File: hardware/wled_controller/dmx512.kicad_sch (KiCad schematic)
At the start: 12 parts, among them J18 NC3MAH, J19 NC3FAH, U10 TLV74333, U9 ISO35T

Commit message: finalise schematic
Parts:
- U9: Shop (none) -> https://eu.mouser.com/ProductDetail/Texas-Instruments/ISO35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
- renumbered J18 to J21, J19 to J22
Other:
- note added: "TODO: decide whether to use 3-pin or 5-pin connectors"
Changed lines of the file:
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@@
+	)
+	(junction
+		(at 114.3 80.01)
+		(diameter 0)
+		(color 0 0 0 0)
 	)
 	(junction
@@
 	)
 	(junction
+		(at 132.08 60.96)
+		(diameter 0)
+		(color 0 0 0 0)
+	)
+	(junction
 		(at 121.92 111.76)
 		(diameter 0)
@@
 	(wire
 		(pts
+			(xy 114.3 80.01) (xy 110.49 80.01)
+		)
+		(stroke
+			(width 0)
+			(type default)
+		)
+	)
+	(wire
+		(pts
 			(xy 185.42 60.96) (xy 180.34 60.96)
 		)
@@
 	(wire
 		(pts
-			(xy 137.16 80.01) (xy 110.49 80.01)
+			(xy 137.16 80.01) (xy 114.3 80.01)
 		)
 		(stroke
@@
 	(wire
 		(pts
+			(xy 114.3 78.74) (xy 114.3 80.01)
+		)
+		(stroke
+			(width 0)
+			(type default)
+		)
+	)
+	(wire
+		(pts
 			(xy 77.47 109.22) (xy 77.47 85.09)
 		)
@@
 	(wire
 		(pts
+			(xy 130.81 60.96) (xy 132.08 60.96)
+		)
+		(stroke
+			(width 0)
+			(type default)
+		)
+	)
+	(wire
+		(pts
 			(xy 90.17 129.54) (xy 91.44 129.54)
 		)
@@
 			(width 0)
 			(type default)
+		)
+	)
+	(text "TODO: decide whether to use 3-pin or 5-pin connectors"
+		(exclude_from_sim no)
+		(at 222.25 38.1 0)
+		(effects
+			(font
+				(size 1.27 1.27)
+			)
 		)
 	)
@@
 			)
 			(justify right)
+		)
+	)
+	(symbol
+		(lib_id "power:PWR_FLAG")
+		(at 114.3 78.74 0)
+		(unit 1)
+		(exclude_from_sim no)
+		(in_bom yes)
+		(on_board yes)
+		(dnp no)
+		(fields_autoplaced yes)
+		(property "Reference" "#FLG06"
+			(at 114.3 76.835 0)
+			(effects
+				(font
+					(size 1.27 1.27)
+				)
+				(hide yes)
+			)
+		)
+		(property "Value" "PWR_FLAG"
+			(at 114.3 73.66 0)
+			(effects
+				(font
+					(size 1.27 1.27)
+				)
+				(hide yes)
+			)
+		)
+		(property "Footprint" ""
+			(at 114.3 78.74 0)
+			(effects
+				(font
+					(size 1.27 1.27)
+				)
+				(hide yes)
+			)
+		)
+		(property "Datasheet" "~"
+			(at 114.3 78.74 0)
+			(effects
+				(font
+					(size 1.27 1.27)
+				)
+				(hide yes)
+			)
+		)
+		(property "Description" "Special symbol for telling ERC where power comes from"
+			(at 114.3 78.74 0)
+			(effects
+				(font
+					(size 1.27 1.27)
+				)
+				(hide yes)
+			)
+		)
+		(pin "1"
+		)
+		(instances
+			(project "wled_controller"
+				(path "/67a034fd-c582-46b2-83e2-3de9f5f70ac4/ded7ca3b-172a-4291-b42a-ac8e31eb8d0c"
+					(reference "#FLG06")
+					(unit 1)
+				)
+			)
 		)
 	)
@@
 		(dnp no)
 		(fields_autoplaced yes)
-		(property "Reference" "#PWR091"
+		(property "Reference" "#PWR097"
 			(at 39.37 97.79 0)
 			(effects
@@
 			(project "wled_controller"
 				(path "/67a034fd-c582-46b2-83e2-3de9f5f70ac4/ded7ca3b-172a-4291-b42a-ac8e31eb8d0c"
-					(reference "#PWR091")
+					(reference "#PWR097")
 					(unit 1)
 				)
@@
 		(dnp no)
 		(fields_autoplaced yes)
-		(property "Reference" "J18"
+		(property "Reference" "J21"
 			(at 227.33 49.53 0)
 			(effects
@@
 			(project ""
 				(path "/67a034fd-c582-46b2-83e2-3de9f5f70ac4/ded7ca3b-172a-4291-b42a-ac8e31eb8d0c"
-					(reference "J18")
+					(reference "J21")
 					(unit 1)
 				)
@@
 		(on_board yes)
 		(dnp no)
-		(property "Reference" "#PWR090"
+		(property "Reference" "#PWR096"
 			(at 39.37 82.55 0)
 			(effects
@@
 			(project "wled_controller"
 				(path "/67a034fd-c582-46b2-83e2-3de9f5f70ac4/ded7ca3b-172a-4291-b42a-ac8e31eb8d0c"
-					(reference "#PWR090")
+					(reference "#PWR096")
 					(unit 1)
 				)
@@
 		(dnp no)
 		(fields_autoplaced yes)
-		(property "Reference" "#PWR095"
+		(property "Reference" "#PWR0101"
 			(at 83.82 129.54 0)
 			(effects
@@
 			(project "wled_controller"
 				(path "/67a034fd-c582-46b2-83e2-3de9f5f70ac4/ded7ca3b-172a-4291-b42a-ac8e31eb8d0c"
-					(reference "#PWR095")
+					(reference "#PWR0101")
 					(unit 1)
 				)
@@
 	)
 	(symbol
+		(lib_id "power:PWR_FLAG")
+		(at 130.81 60.96 90)
+		(unit 1)
+		(exclude_from_sim no)
+		(in_bom yes)
+		(on_board yes)
+		(dnp no)
+		(fields_autoplaced yes)
+		(property "Reference" "#FLG07"
+			(at 128.905 60.96 0)
+			(effects
+				(font
+					(size 1.27 1.27)
+				)
+				(hide yes)
+			)
+		)
+		(property "Value" "PWR_FLAG"
+			(at 125.73 60.96 0)
+			(effects
+				(font
+					(size 1.27 1.27)
+				)
+				(hide yes)
+			)
+		)
+		(property "Footprint" ""
+			(at 130.81 60.96 0)
+			(effects
+				(font
+					(size 1.27 1.27)
+				)
+				(hide yes)
+			)
+		)
+		(property "Datasheet" "~"
+			(at 130.81 60.96 0)
+			(effects
+				(font
+					(size 1.27 1.27)
+				)
+				(hide yes)
+			)
+		)
+		(property "Description" "Special symbol for telling ERC where power comes from"
+			(at 130.81 60.96 0)
+			(effects
+				(font
+					(size 1.27 1.27)
+				)
+				(hide yes)
+			)
+		)
+		(pin "1"
+		)
+		(instances
+			(project "wled_controller"
+				(path "/67a034fd-c582-46b2-83e2-3de9f5f70ac4/ded7ca3b-172a-4291-b42a-ac8e31eb8d0c"
+					(reference "#FLG07")
+					(unit 1)
+				)
+			)
+		)
+	)
+	(symbol
 		(lib_id "power:+3.3V")
 		(at 88.9 80.01 90)
@@
 		(dnp no)
 		(fields_autoplaced yes)
-		(property "Reference" "#PWR092"
+		(property "Reference" "#PWR098"
 			(at 92.71 80.01 0)
 			(effects
@@
 			(project "wled_controller"
 				(path "/67a034fd-c582-46b2-83e2-3de9f5f70ac4/ded7ca3b-172a-4291-b42a-ac8e31eb8d0c"
-					(reference "#PWR092")
+					(reference "#PWR098")
 					(unit 1)
 				)
@@
 		(dnp no)
 		(fields_autoplaced yes)
-		(property "Reference" "#PWR093"
+		(property "Reference" "#PWR099"
 			(at 92.71 104.14 0)
 			(effects
@@
 			(project ""
 				(path "/67a034fd-c582-46b2-83e2-3de9f5f70ac4/ded7ca3b-172a-4291-b42a-ac8e31eb8d0c"
-					(reference "#PWR093")
+					(reference "#PWR099")
 					(unit 1)
 				)
@@
 		(dnp no)
 		(fields_autoplaced yes)
-		(property "Reference" "J19"
+		(property "Reference" "J22"
 			(at 227.33 74.93 0)
 			(effects
@@
 			(project ""
 				(path "/67a034fd-c582-46b2-83e2-3de9f5f70ac4/ded7ca3b-172a-4291-b42a-ac8e31eb8d0c"
-					(reference "J19")
+					(reference "J22")
 					(unit 1)
 				)
@@
 			)
 		)
+		(property "Shop" "https://eu.mouser.com/ProductDetail/Texas-Instruments/ISO35TDWR?qs=QtI0yD1FyONZngHt9P0v7A%3D%3D"
+			(at 105.41 101.6 0)
+			(effects
+				(font
+					(size 1.27 1.27)
+				)
+				(hide yes)
+			)
+		)
 		(pin "4"
 		)
@@
 		(dnp no)
 		(fields_autoplaced yes)
-		(property "Reference" "#PWR094"
+		(property "Reference" "#PWR0100"
 			(at 90.17 102.87 0)
 			(effects
@@
 			(project "wled_controller"
 				(path "/67a034fd-c582-46b2-83e2-3de9f5f70ac4/ded7ca3b-172a-4291-b42a-ac8e31eb8d0c"
-					(reference "#PWR094")
+					(reference "#PWR0100")
 					(unit 1)
 				)

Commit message: some progress on PCB
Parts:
- removed C13: 100nF, Capacitor_SMD:C_0805_2012Metric, symbol Device:C
- renumbered C14 to C13, C15 to C14, C16 to C15, C17 to C16, C18 to C17, D3 to D4

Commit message: work on pcb
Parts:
- renumbered C13 to C11, C14 to C12, C15 to C13, C16 to C14, C17 to C15
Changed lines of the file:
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@@
 		(on_board yes)
 		(dnp no)
-		(property "Reference" "C13"
+		(property "Reference" "C11"
 			(at 91.44 88.9 0)
 			(effects
@@
 			(project "wled_controller"
 				(path "/67a034fd-c582-46b2-83e2-3de9f5f70ac4/ded7ca3b-172a-4291-b42a-ac8e31eb8d0c"
-					(reference "C13")
+					(reference "C11")
 					(unit 1)
 				)
@@
 		(on_board yes)
 		(dnp no)
-		(property "Reference" "C14"
+		(property "Reference" "C12"
 			(at 138.43 67.31 0)
 			(effects
@@
 			(project "wled_controller"
 				(path "/67a034fd-c582-46b2-83e2-3de9f5f70ac4/ded7ca3b-172a-4291-b42a-ac8e31eb8d0c"
-					(reference "C14")
+					(reference "C12")
 					(unit 1)
 				)
@@
 		(on_board yes)
 		(dnp no)
-		(property "Reference" "C17"
+		(property "Reference" "C15"
 			(at 186.69 67.31 0)
 			(effects
@@
 			(project "wled_controller"
 				(path "/67a034fd-c582-46b2-83e2-3de9f5f70ac4/ded7ca3b-172a-4291-b42a-ac8e31eb8d0c"
-					(reference "C17")
+					(reference "C15")
 					(unit 1)
 				)
@@
 		(on_board yes)
 		(dnp no)
-		(property "Reference" "C15"
+		(property "Reference" "C13"
 			(at 148.59 67.31 0)
 			(effects
@@
 			(project "wled_controller"
 				(path "/67a034fd-c582-46b2-83e2-3de9f5f70ac4/ded7ca3b-172a-4291-b42a-ac8e31eb8d0c"
-					(reference "C15")
+					(reference "C13")
 					(unit 1)
 				)
@@
 		(on_board yes)
 		(dnp no)
-		(property "Reference" "C16"
+		(property "Reference" "C14"
 			(at 158.75 67.31 0)
 			(effects
@@
 			(project "wled_controller"
 				(path "/67a034fd-c582-46b2-83e2-3de9f5f70ac4/ded7ca3b-172a-4291-b42a-ac8e31eb8d0c"
-					(reference "C16")
+					(reference "C14")
 					(unit 1)
 				)
@@
 		(dnp no)
 		(fields_autoplaced yes)
-		(property "Reference" "#PWR099"
+		(property "Reference" "#PWR096"
 			(at 83.82 129.54 0)
 			(effects
@@
 			(project "wled_controller"
 				(path "/67a034fd-c582-46b2-83e2-3de9f5f70ac4/ded7ca3b-172a-4291-b42a-ac8e31eb8d0c"
-					(reference "#PWR099")
+					(reference "#PWR096")
 					(unit 1)
 				)
@@
 		(dnp no)
 		(fields_autoplaced yes)
-		(property "Reference" "#PWR096"
+		(property "Reference" "#PWR093"
 			(at 92.71 80.01 0)
 			(effects
@@
 			(project "wled_controller"
 				(path "/67a034fd-c582-46b2-83e2-3de9f5f70ac4/ded7ca3b-172a-4291-b42a-ac8e31eb8d0c"
-					(reference "#PWR096")
+					(reference "#PWR093")
 					(unit 1)
 				)
@@
 		(dnp no)
 		(fields_autoplaced yes)
-		(property "Reference" "#PWR097"
+		(property "Reference" "#PWR094"
 			(at 92.71 104.14 0)
 			(effects
@@
 			(project ""
 				(path "/67a034fd-c582-46b2-83e2-3de9f5f70ac4/ded7ca3b-172a-4291-b42a-ac8e31eb8d0c"
-					(reference "#PWR097")
+					(reference "#PWR094")
 					(unit 1)
 				)
@@
 		(dnp no)
 		(fields_autoplaced yes)
-		(property "Reference" "#PWR098"
+		(property "Reference" "#PWR095"
 			(at 90.17 102.87 0)
 			(effects
@@
 			(project "wled_controller"
 				(path "/67a034fd-c582-46b2-83e2-3de9f5f70ac4/ded7ca3b-172a-4291-b42a-ac8e31eb8d0c"
-					(reference "#PWR098")
-					(unit 1)
-				)
+					(reference "#PWR095")
+					(unit 1)
+				)

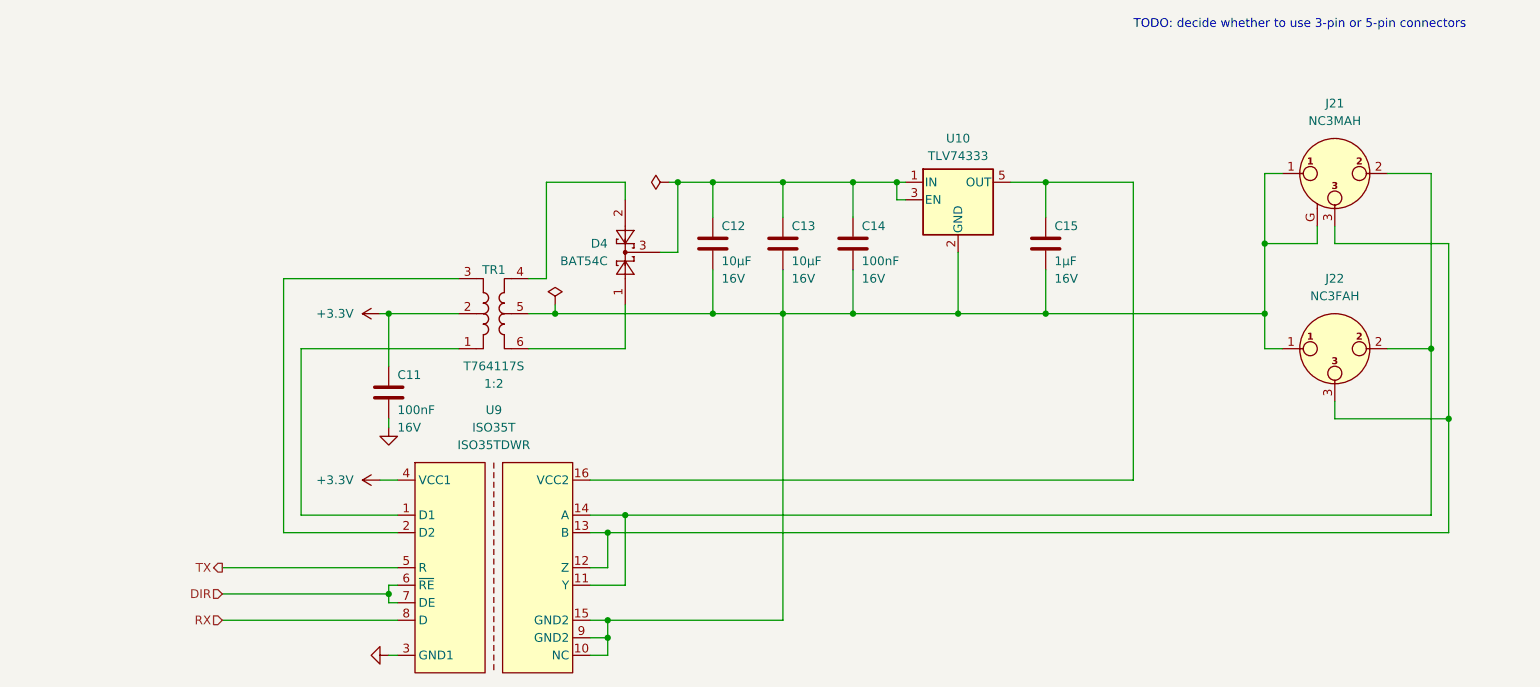
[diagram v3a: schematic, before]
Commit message: dmx512 line TVS
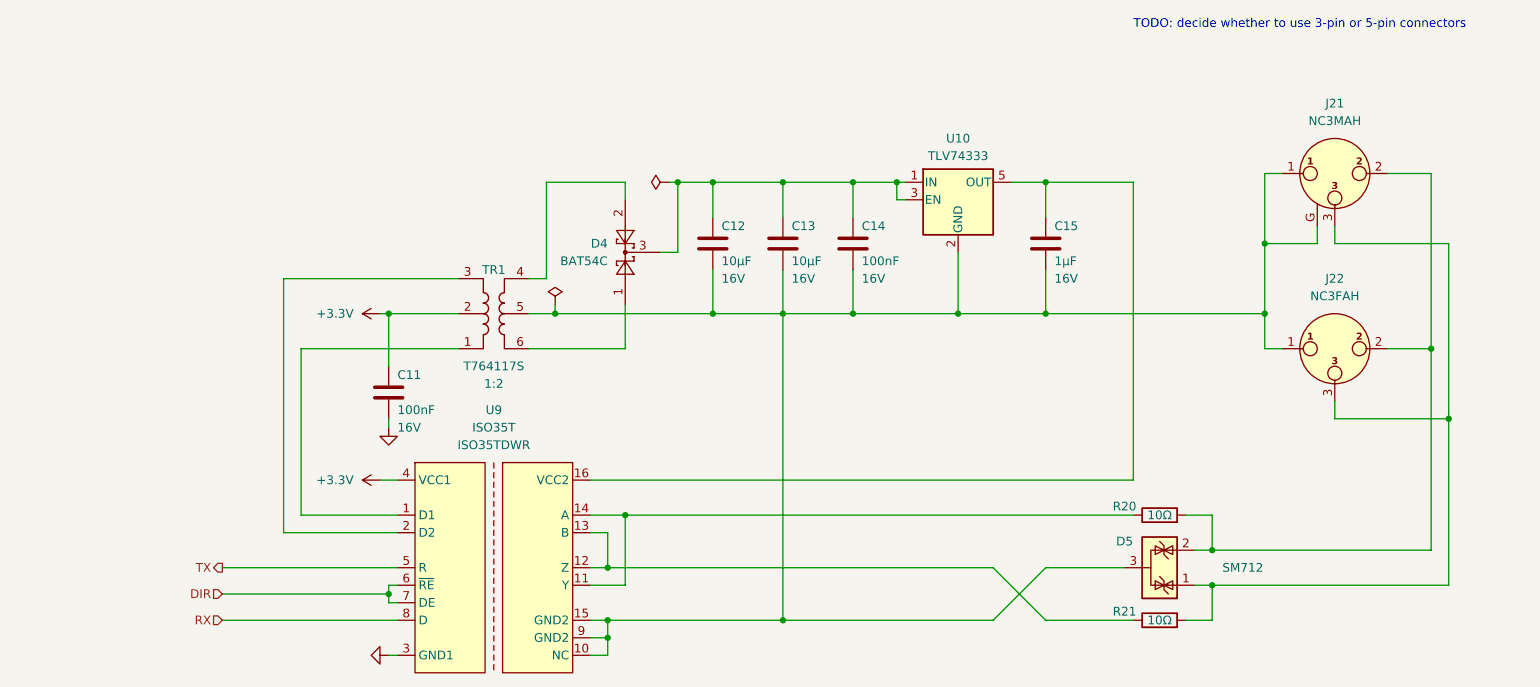
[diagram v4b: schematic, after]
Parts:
- added D5: SM712, Package_TO_SOT_SMD:SOT-23, symbol Power_Protection:NUP2105L
- added R20, R21: 10Ω, Resistor_SMD:R_0805_2012Metric, symbol Device:R
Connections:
- net at C12.2, C13.2, C14.2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: now also D5.3 (A)
- net at J21.2, J22.2: now also D5.2 (K), R20.2; no longer U9.11 (Y), U9.14 (A)
- net at J21.3, J22.3: now also D5.1 (K), R21.2; no longer U9.12 (Z), U9.13 (B)
- new net: R20.1, U9.11 (Y), U9.14 (A)
- new net: R21.1, U9.12 (Z), U9.13 (B)

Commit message: update bom
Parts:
- D5: Part (none) -> SM712
- R20, R21: Part (none) -> R 10Ω 125mW 5% 0805
- TR1: Part PAD001-T764120S -> PAD001-T764120S
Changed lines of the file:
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@@
 		)
 		(instances
-			(project ""
+			(project "wled_controller"
 				(path "/67a034fd-c582-46b2-83e2-3de9f5f70ac4/ded7ca3b-172a-4291-b42a-ac8e31eb8d0c"
 					(reference "J21")
@@
 		)
 		(property "Shop" "https://store.comet.bg/Catalogue/Product/29580/"
+			(at 201.93 109.22 0)
+			(effects
+				(font
+					(size 1.27 1.27)
+				)
+				(hide yes)
+			)
+		)
+		(property "Part" "R 10Ω 125mW 5% 0805"
 			(at 201.93 109.22 0)
 			(effects
@@
 			)
 		)
+		(property "Part" "SM712"
+			(at 201.93 116.84 0)
+			(effects
+				(font
+					(size 1.27 1.27)
+				)
+				(hide yes)
+			)
+		)
 		(pin "3"
 		)
@@
 			)
 		)
-		(property "Part" " PAD001-T764120S"
+		(property "Part" "PAD001-T764120S"
 			(at 105.41 80.01 0)
 			(effects
@@
 		)
 		(instances
-			(project ""
+			(project "wled_controller"
 				(path "/67a034fd-c582-46b2-83e2-3de9f5f70ac4/ded7ca3b-172a-4291-b42a-ac8e31eb8d0c"
 					(reference "TR1")
@@
 		)
 		(instances
-			(project ""
+			(project "wled_controller"
 				(path "/67a034fd-c582-46b2-83e2-3de9f5f70ac4/ded7ca3b-172a-4291-b42a-ac8e31eb8d0c"
 					(reference "#PWR095")
@@
 		)
 		(instances
-			(project ""
+			(project "wled_controller"
 				(path "/67a034fd-c582-46b2-83e2-3de9f5f70ac4/ded7ca3b-172a-4291-b42a-ac8e31eb8d0c"
 					(reference "J22")
@@
 		)
 		(instances
-			(project ""
+			(project "wled_controller"
 				(path "/67a034fd-c582-46b2-83e2-3de9f5f70ac4/ded7ca3b-172a-4291-b42a-ac8e31eb8d0c"
 					(reference "U9")
@@
 		)
 		(instances
-			(project ""
+			(project "wled_controller"
 				(path "/67a034fd-c582-46b2-83e2-3de9f5f70ac4/ded7ca3b-172a-4291-b42a-ac8e31eb8d0c"
 					(reference "D4")
@@
 		)
 		(property "Shop" "https://store.comet.bg/Catalogue/Product/29580/"
+			(at 201.93 124.46 0)
+			(effects
+				(font
+					(size 1.27 1.27)
+				)
+				(hide yes)
+			)
+		)
+		(property "Part" "R 10Ω 125mW 5% 0805"
 			(at 201.93 124.46 0)
 			(effects
@@
 		)
 		(instances
-			(project ""
+			(project "wled_controller"
 				(path "/67a034fd-c582-46b2-83e2-3de9f5f70ac4/ded7ca3b-172a-4291-b42a-ac8e31eb8d0c"
 					(reference "U10")
